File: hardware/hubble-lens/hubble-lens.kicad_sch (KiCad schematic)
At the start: 54 parts, among them J1 Eurorack Power, J10 MIX, J101 Left, J102 Bottom, J103 Right, J104 SWD, J105 USB, J3 CASTOR PITCH, J4 POLLUX PITCH, J5 CASTOR DUTY, J6 POLLUX DUTY, J7 CASTOR OUT, J8 POLLUX OUT, SW2 BUTTON

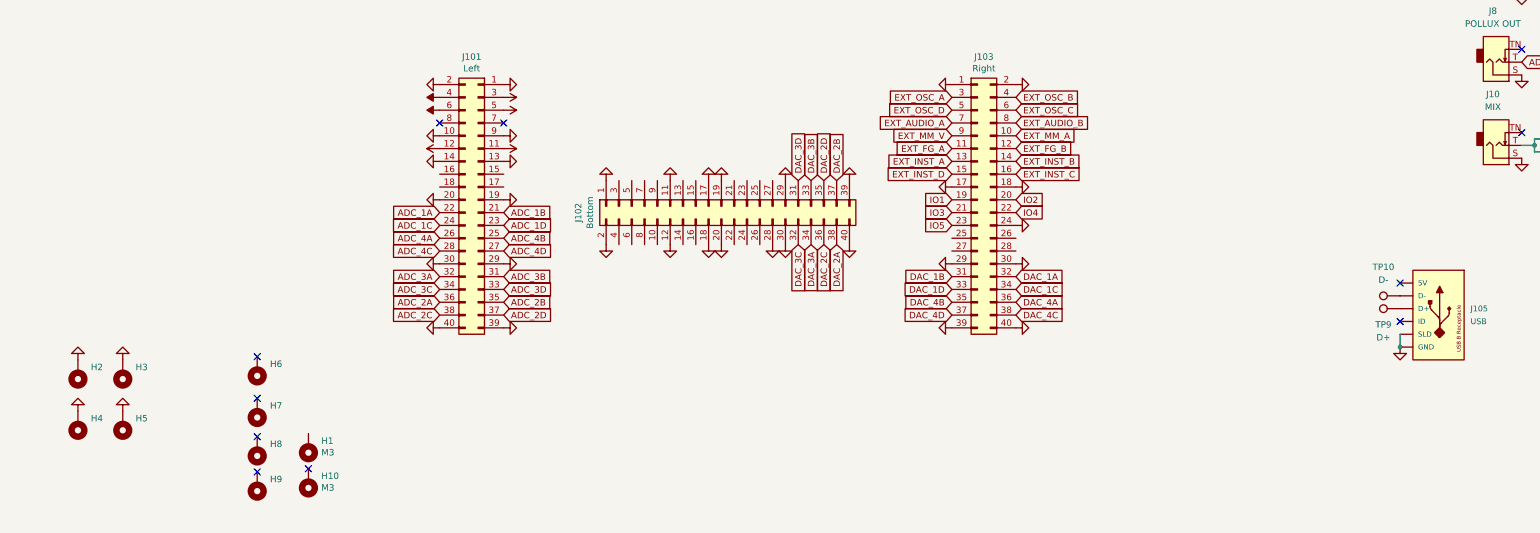
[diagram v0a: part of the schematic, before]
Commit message: update hubble-lens to kicad 9
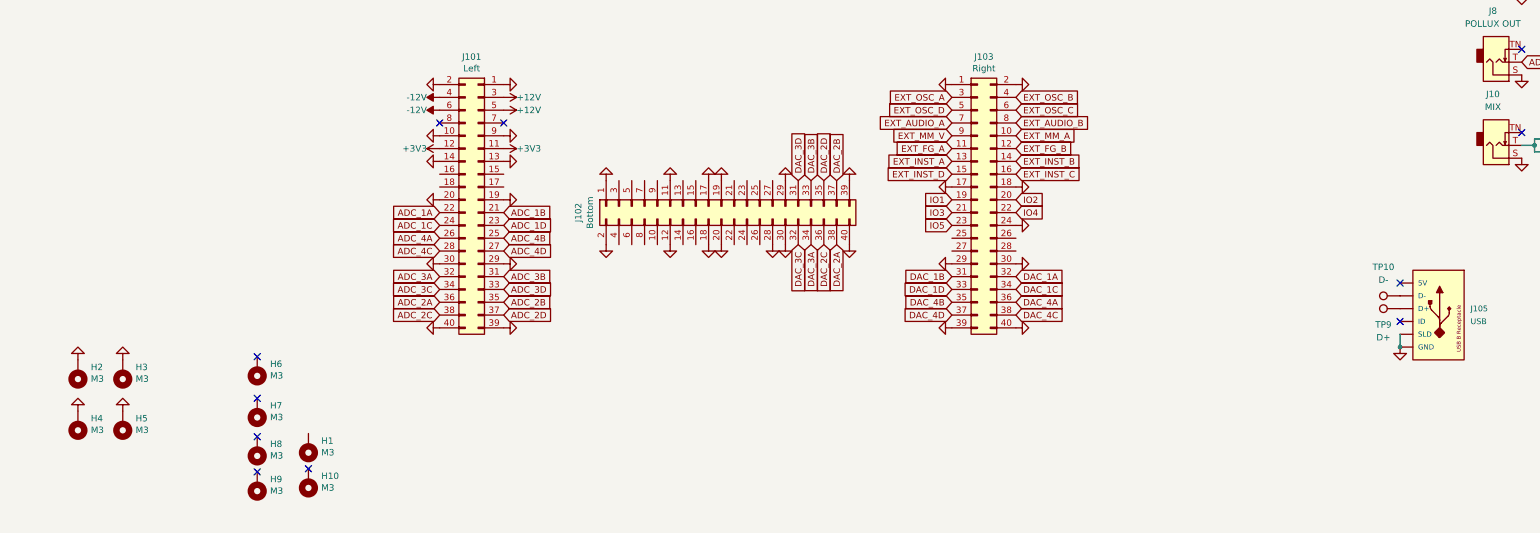
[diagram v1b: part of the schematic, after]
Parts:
- H2, H3, H4, H5, H6, H7, H8, H9: value (none) -> M3
